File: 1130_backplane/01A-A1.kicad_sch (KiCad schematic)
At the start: 86 parts

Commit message: DN101-DN111 added to backplane schematics, DN111 01B-A1 connections made, 01B-B1 connections to be made when all signals on connectors
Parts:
- removed J1, J10, J11, J12, J13, J14, J15, J16, J17, J18, J19, J2, J20, J21, J22, J23, J24, J25, J26, J27, J28, J29, J3, J30, J31, J32, J33, J34, J35, J36, J37, J38, J39, J4, J40, J41, J42, J43, J44, J45, J46, J47, J48, J49, J5, J50, J51, J52, J53, J54, J55, J56, J57, J58, J59, J6, J60, J61, J62, J63, J64, J65, J66, J67, J68, J69, J7, J70, J71, J72, J73, J74, J75, J76, J77, J78, J79, J8, J80, J81, J82, J83, J84, J85, J86, J9: ~, symbol Connector_Generic:Conn_02x12_Row_Letter_First
- added J? (x86): ~, symbol Connector_Generic:Conn_02x12_Row_Letter_First
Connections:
- net +3V: now also J?.b2 (Pin_b2), J?.b2 (Pin_b2), J?.b2 (Pin_b2), J?.b2 (Pin_b2), J?.b2 (Pin_b2), J?.b2 (Pin_b2), J?.b2 (Pin_b2), J?.b2 (Pin_b2), J?.b2 (Pin_b2), J?.b2 (Pin_b2), J?.b2 (Pin_b2), J?.b2 (Pin_b2), J?.b2 (Pin_b2), J?.b2 (Pin_b2), J?.b2 (Pin_b2), J?.b2 (Pin_b2), J?.b2 (Pin_b2), J?.b2 (Pin_b2), J?.b2 (Pin_b2), J?.b2 (Pin_b2), J?.b2 (Pin_b2), J?.b2 (Pin_b2), J?.b2 (Pin_b2), J?.b2 (Pin_b2), J?.b2 (Pin_b2), J?.b2 (Pin_b2), J?.b2 (Pin_b2), J?.b2 (Pin_b2), J?.b2 (Pin_b2), J?.b2 (Pin_b2), J?.b2 (Pin_b2), J?.b2 (Pin_b2), J?.b2 (Pin_b2), J?.b2 (Pin_b2), J?.b2 (Pin_b2), J?.b2 (Pin_b2), J?.b2 (Pin_b2), J?.b2 (Pin_b2), J?.b2 (Pin_b2), J?.b2 (Pin_b2), J?.b2 (Pin_b2), J?.b2 (Pin_b2), J?.b2 (Pin_b2), J?.b2 (Pin_b2), J?.b2 (Pin_b2), J?.b2 (Pin_b2), J?.b2 (Pin_b2), J?.b2 (Pin_b2), J?.b2 (Pin_b2), J?.b2 (Pin_b2), J?.b2 (Pin_b2), J?.b2 (Pin_b2), J?.b2 (Pin_b2), J?.b2 (Pin_b2), J?.b2 (Pin_b2), J?.b2 (Pin_b2), J?.b2 (Pin_b2), J?.b2 (Pin_b2), J?.b2 (Pin_b2), J?.b2 (Pin_b2), J?.b2 (Pin_b2), J?.b2 (Pin_b2), J?.b2 (Pin_b2), J?.b2 (Pin_b2), J?.b2 (Pin_b2), J?.b2 (Pin_b2), J?.b2 (Pin_b2), J?.b2 (Pin_b2), J?.b2 (Pin_b2), J?.b2 (Pin_b2), J?.b2 (Pin_b2), J?.b2 (Pin_b2), J?.b2 (Pin_b2), J?.b2 (Pin_b2), J?.b2 (Pin_b2), J?.b2 (Pin_b2), J?.b2 (Pin_b2)
- net +6V: now also J?.a10 (Pin_a10), J?.a10 (Pin_a10), J?.a10 (Pin_a10), J?.a10 (Pin_a10), J?.a10 (Pin_a10), J?.a10 (Pin_a10), J?.a10 (Pin_a10), J?.a10 (Pin_a10), J?.a10 (Pin_a10), J?.a10 (Pin_a10), J?.a10 (Pin_a10), J?.a10 (Pin_a10), J?.a10 (Pin_a10), J?.a10 (Pin_a10), J?.a10 (Pin_a10), J?.a10 (Pin_a10), J?.a10 (Pin_a10), J?.a10 (Pin_a10), J?.a10 (Pin_a10), J?.a10 (Pin_a10), J?.a10 (Pin_a10), J?.a10 (Pin_a10), J?.a10 (Pin_a10), J?.a10 (Pin_a10), J?.a10 (Pin_a10), J?.a10 (Pin_a10), J?.a10 (Pin_a10), J?.a10 (Pin_a10), J?.a10 (Pin_a10), J?.a10 (Pin_a10), J?.a10 (Pin_a10), J?.a10 (Pin_a10), J?.a10 (Pin_a10), J?.a10 (Pin_a10), J?.a10 (Pin_a10), J?.a10 (Pin_a10), J?.a10 (Pin_a10), J?.a10 (Pin_a10), J?.a10 (Pin_a10), J?.a10 (Pin_a10), J?.a10 (Pin_a10), J?.a10 (Pin_a10), J?.a10 (Pin_a10), J?.a10 (Pin_a10), J?.a10 (Pin_a10), J?.a10 (Pin_a10), J?.a10 (Pin_a10), J?.a10 (Pin_a10), J?.a10 (Pin_a10), J?.a10 (Pin_a10), J?.a10 (Pin_a10), J?.a10 (Pin_a10), J?.a10 (Pin_a10), J?.a10 (Pin_a10), J?.a10 (Pin_a10), J?.a10 (Pin_a10), J?.a10 (Pin_a10), J?.a10 (Pin_a10), J?.a10 (Pin_a10), J?.a10 (Pin_a10), J?.a10 (Pin_a10), J?.a10 (Pin_a10), J?.a10 (Pin_a10), J?.a10 (Pin_a10), J?.a10 (Pin_a10), J?.a10 (Pin_a10), J?.a10 (Pin_a10), J?.a10 (Pin_a10), J?.a10 (Pin_a10), J?.a10 (Pin_a10), J?.a10 (Pin_a10), J?.a10 (Pin_a10), J?.a10 (Pin_a10), J?.a10 (Pin_a10), J?.a10 (Pin_a10), J?.a10 (Pin_a10), J?.a10 (Pin_a10)
- net -3V: now also J?.a5 (Pin_a5), J?.a5 (Pin_a5), J?.a5 (Pin_a5), J?.a5 (Pin_a5), J?.a5 (Pin_a5), J?.a5 (Pin_a5), J?.a5 (Pin_a5), J?.a5 (Pin_a5), J?.a5 (Pin_a5), J?.a5 (Pin_a5), J?.a5 (Pin_a5), J?.a5 (Pin_a5), J?.a5 (Pin_a5), J?.a5 (Pin_a5), J?.a5 (Pin_a5), J?.a5 (Pin_a5), J?.a5 (Pin_a5), J?.a5 (Pin_a5), J?.a5 (Pin_a5), J?.a5 (Pin_a5), J?.a5 (Pin_a5), J?.a5 (Pin_a5), J?.a5 (Pin_a5), J?.a5 (Pin_a5), J?.a5 (Pin_a5), J?.a5 (Pin_a5), J?.a5 (Pin_a5), J?.a5 (Pin_a5), J?.a5 (Pin_a5), J?.a5 (Pin_a5), J?.a5 (Pin_a5), J?.a5 (Pin_a5), J?.a5 (Pin_a5), J?.a5 (Pin_a5), J?.a5 (Pin_a5), J?.a5 (Pin_a5), J?.a5 (Pin_a5), J?.a5 (Pin_a5), J?.a5 (Pin_a5), J?.a5 (Pin_a5), J?.a5 (Pin_a5), J?.a5 (Pin_a5), J?.a5 (Pin_a5), J?.a5 (Pin_a5), J?.a5 (Pin_a5), J?.a5 (Pin_a5), J?.a5 (Pin_a5), J?.a5 (Pin_a5), J?.a5 (Pin_a5), J?.a5 (Pin_a5), J?.a5 (Pin_a5), J?.a5 (Pin_a5), J?.a5 (Pin_a5), J?.a5 (Pin_a5), J?.a5 (Pin_a5), J?.a5 (Pin_a5), J?.a5 (Pin_a5), J?.a5 (Pin_a5), J?.a5 (Pin_a5), J?.a5 (Pin_a5), J?.a5 (Pin_a5), J?.a5 (Pin_a5), J?.a5 (Pin_a5), J?.a5 (Pin_a5), J?.a5 (Pin_a5), J?.a5 (Pin_a5), J?.a5 (Pin_a5), J?.a5 (Pin_a5), J?.a5 (Pin_a5), J?.a5 (Pin_a5), J?.a5 (Pin_a5), J?.a5 (Pin_a5), J?.a5 (Pin_a5), J?.a5 (Pin_a5), J?.a5 (Pin_a5), J?.a5 (Pin_a5), J?.a5 (Pin_a5)
- net -IO_BIT_0: now also J?.a2 (Pin_a2)
- net -IO_BIT_1: now also J?.b1 (Pin_b1)
- net -IO_BIT_10: now also J?.a7 (Pin_a7)
- net -IO_BIT_11: now also J?.b6 (Pin_b6)
- net -IO_BIT_12: now also J?.a8 (Pin_a8)
- net -IO_BIT_13: now also J?.b8 (Pin_b8)
- net -IO_BIT_14: now also J?.a9 (Pin_a9)
- net -IO_BIT_15: now also J?.b9 (Pin_b9)
- net -IO_BIT_2: now also J?.a3 (Pin_a3)
- net -IO_BIT_3: now also J?.b2 (Pin_b2)
- net -IO_BIT_4: now also J?.a4 (Pin_a4)
- net -IO_BIT_5: now also J?.b3 (Pin_b3)
- net -IO_BIT_6: now also J?.a5 (Pin_a5)
- net -IO_BIT_7: now also J?.b4 (Pin_b4)
- net -IO_BIT_8: now also J?.a6 (Pin_a6)
- net -IO_BIT_9: now also J?.b5 (Pin_b5)
- net GND: now also J?.b7 (Pin_b7), J?.b7 (Pin_b7), J?.b7 (Pin_b7), J?.b7 (Pin_b7), J?.b7 (Pin_b7), J?.b7 (Pin_b7), J?.b7 (Pin_b7), J?.b7 (Pin_b7), J?.b7 (Pin_b7), J?.b7 (Pin_b7), J?.b7 (Pin_b7), J?.b7 (Pin_b7), J?.b7 (Pin_b7), J?.b7 (Pin_b7), J?.b7 (Pin_b7), J?.b7 (Pin_b7), J?.b7 (Pin_b7), J?.b7 (Pin_b7), J?.b7 (Pin_b7), J?.b7 (Pin_b7), J?.b7 (Pin_b7), J?.b7 (Pin_b7), J?.b7 (Pin_b7), J?.b7 (Pin_b7), J?.b7 (Pin_b7), J?.b7 (Pin_b7), J?.b7 (Pin_b7), J?.b7 (Pin_b7), J?.b7 (Pin_b7), J?.b7 (Pin_b7), J?.b7 (Pin_b7), J?.b7 (Pin_b7), J?.b7 (Pin_b7), J?.b7 (Pin_b7), J?.b7 (Pin_b7), J?.b7 (Pin_b7), J?.b7 (Pin_b7), J?.b7 (Pin_b7), J?.b7 (Pin_b7), J?.b7 (Pin_b7), J?.b7 (Pin_b7), J?.b7 (Pin_b7), J?.b7 (Pin_b7), J?.b7 (Pin_b7), J?.b7 (Pin_b7), J?.b7 (Pin_b7), J?.b7 (Pin_b7), J?.b7 (Pin_b7), J?.b7 (Pin_b7), J?.b7 (Pin_b7), J?.b7 (Pin_b7), J?.b7 (Pin_b7), J?.b7 (Pin_b7), J?.b7 (Pin_b7), J?.b7 (Pin_b7), J?.b7 (Pin_b7), J?.b7 (Pin_b7), J?.b7 (Pin_b7), J?.b7 (Pin_b7), J?.b7 (Pin_b7), J?.b7 (Pin_b7), J?.b7 (Pin_b7), J?.b7 (Pin_b7), J?.b7 (Pin_b7), J?.b7 (Pin_b7), J?.b7 (Pin_b7), J?.b7 (Pin_b7), J?.b7 (Pin_b7), J?.b7 (Pin_b7), J?.b7 (Pin_b7), J?.b7 (Pin_b7), J?.b7 (Pin_b7), J?.b7 (Pin_b7), J?.b7 (Pin_b7), J?.b7 (Pin_b7), J?.b7 (Pin_b7), J?.b7 (Pin_b7), J?.b7 (Pin_b7), J?.b7 (Pin_b7), J?.b7 (Pin_b7), J?.b7 (Pin_b7), J?.b7 (Pin_b7), J?.b7 (Pin_b7), J?.b7 (Pin_b7), J?.b7 (Pin_b7), J?.b7 (Pin_b7)

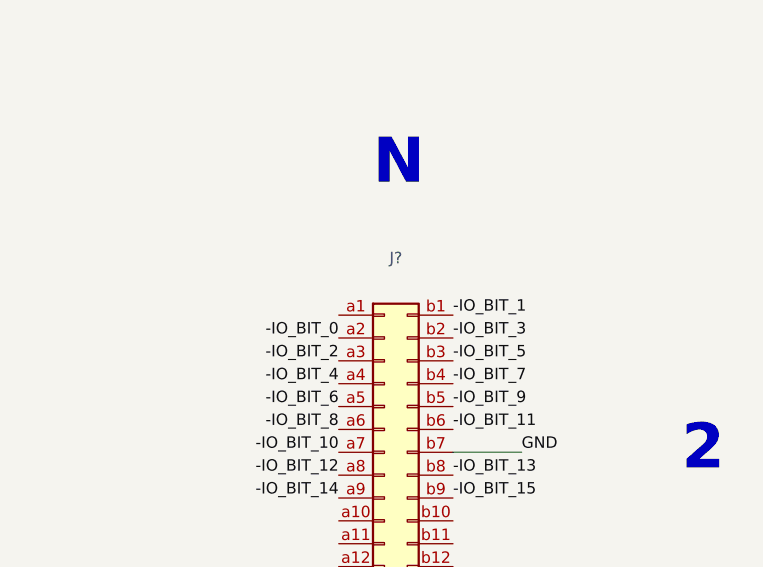
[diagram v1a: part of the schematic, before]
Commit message: Add labels for cable runs, completed tracing for DN111 from previous commit, decided it would be too much work to go back and route later... Completed DN201 page.
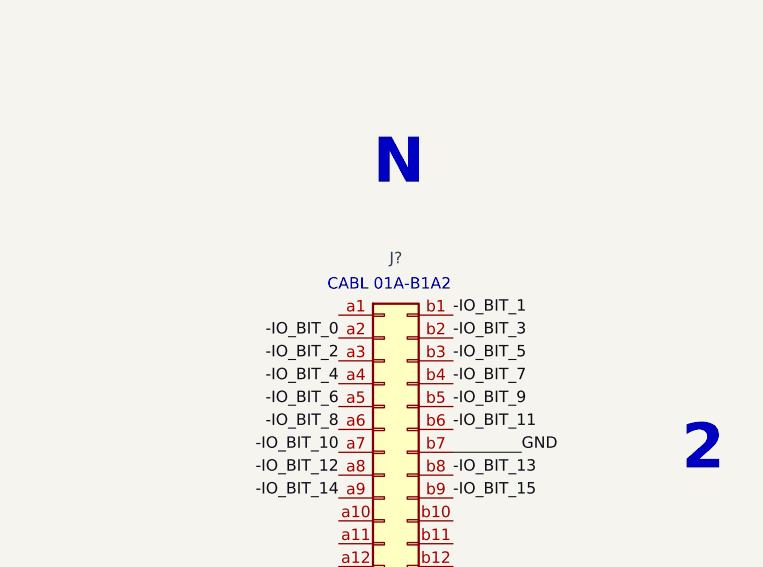
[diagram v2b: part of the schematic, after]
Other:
- note added: "CABL 01A-B1A2"
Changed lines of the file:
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@@
     (effects (font (size 5 5) (thickness 1) bold) (justify left bottom))
+  )
+  (text "CABL 01A-B1A2" (at 793.75 101.6 0)
+    (effects (font (size 1.27 1.27)) (justify left bottom))
   )
   (text "3" (at 833.12 160.02 0)

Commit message: Add labels for bottom T[x] connectors, finished page DU101.
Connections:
- net +3V: no longer J?.b2 (Pin_b2)
- net +6V: no longer J?.a10 (Pin_a10)
- net -3V: no longer J?.a5 (Pin_a5)
- net +U_REG_8_PWR: now reaches J?.a11 (Pin_a11)
- net +U_REG_9_PWR: now reaches J?.a12 (Pin_a12)
- net +XIO_SENSE_ILSW: now reaches J?.a3 (Pin_a3)
- net +XIO_READ: now reaches J?.a7 (Pin_a7)
- net +XIO_CONTROL: now reaches J?.a8 (Pin_a8)
- net +XIO_SENSE_DEVICE: now reaches J?.b9 (Pin_b9)
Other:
- note added: "CABL 01A-B1A5"
- moved on the sheet: J?

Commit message: Fix routing mistake from DU101 for T6, was 01A-A1 to 01A-B1, corrected from 01A-A1 to 01A-C1, finished page DU111.
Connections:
- net +U_REG_13_PWR: now reaches J?.b10 (Pin_b10)
- net +U_REG_14_PWR: now reaches J?.b11 (Pin_b11)
- net +U_REG_15_PWR: now reaches J?.b12 (Pin_b12)
- net +AREA_8: now reaches J?.b3 (Pin_b3)
- net +AREA_6: now reaches J?.a2 (Pin_a2)
- net +XIO_SENSE_RESET_15: now reaches J?.b10 (Pin_b10)
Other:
- note added: "CABL 01A-C1T6"
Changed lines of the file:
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@@
+    (effects (font (size 1.27 1.27)) (justify left bottom))
+  )
+  (text "CABL 01A-C1T6" (at 393.7 393.7 0)
     (effects (font (size 1.27 1.27)) (justify left bottom))
   )
@@
     (effects (font (size 1.27 1.27)) (justify left bottom))
   )
+  (label "+AREA_8" (at 392.43 356.87 90)
+    (effects (font (size 1.27 1.27)) (justify left bottom))
+  )
   (label "GND" (at 370.84 271.78 0)
     (effects (font (size 1.27 1.27)) (justify left bottom))
@@
     (effects (font (size 1.27 1.27)) (justify right bottom))
   )
+  (label "+U_REG_15_PWR" (at 807.72 132.08 0)
+    (effects (font (size 1.27 1.27)) (justify left bottom))
+  )
   (label "GND" (at 434.34 233.68 0)
     (effects (font (size 1.27 1.27)) (justify left bottom))
@@
     (effects (font (size 1.27 1.27)) (justify right bottom))
   )
+  (label "+AREA_6" (at 795.02 220.98 180)
+    (effects (font (size 1.27 1.27)) (justify right bottom))
+  )
   (label "GND" (at 561.34 157.48 0)
     (effects (font (size 1.27 1.27)) (justify left bottom))
@@
     (effects (font (size 1.27 1.27)) (justify right bottom))
   )
+  (label "+U_REG_13_PWR" (at 807.72 127 0)
+    (effects (font (size 1.27 1.27)) (justify left bottom))
+  )
   (label "+3V" (at 307.34 220.98 0)
     (effects (font (size 1.27 1.27)) (justify left bottom))
@@
     (effects (font (size 1.27 1.27)) (justify right bottom))
   )
+  (label "+U_REG_14_PWR" (at 807.72 129.54 0)
+    (effects (font (size 1.27 1.27)) (justify left bottom))
+  )
   (label "+6V" (at 25.4 279.4 180)
     (effects (font (size 1.27 1.27)) (justify right bottom))
@@
     (effects (font (size 1.27 1.27)) (justify right bottom))
   )
+  (label "+XIO_SENSE_RESET_15" (at 807.72 241.3 0)
+    (effects (font (size 1.27 1.27)) (justify left bottom))
+  )
   (label "+6V" (at 279.4 279.4 180)

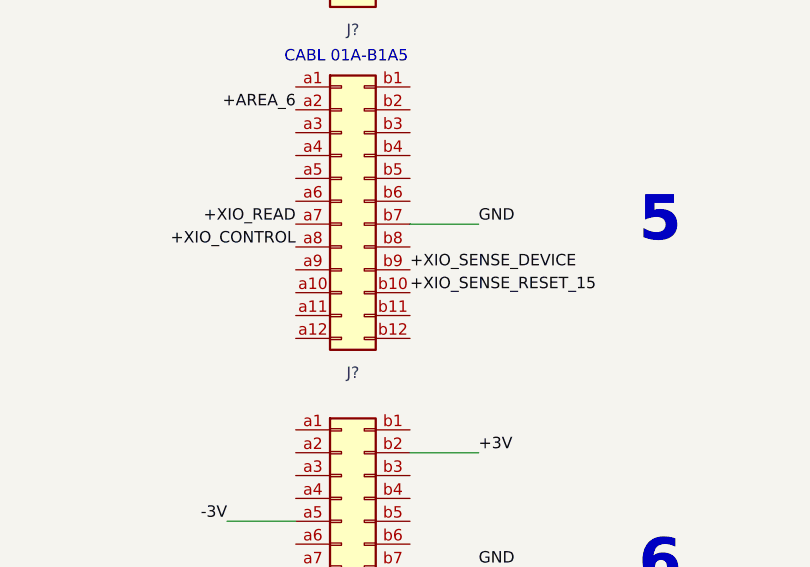
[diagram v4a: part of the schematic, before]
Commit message: Finish page KA101-KA111
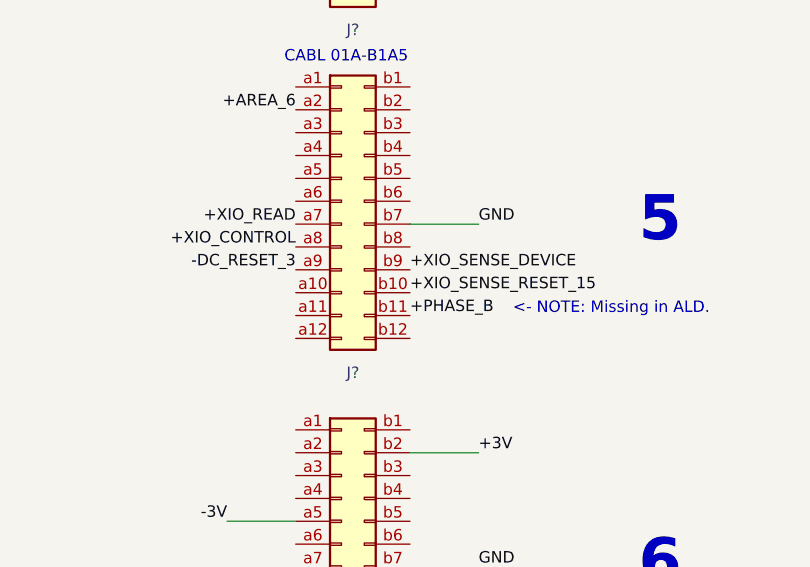
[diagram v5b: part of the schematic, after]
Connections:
- net -DC_RESET_3: now reaches J?.a9 (Pin_a9)
- net +PHASE_B: now reaches J?.b11 (Pin_b11)
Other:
- note added: "<- NOTE: Missing in ALD."
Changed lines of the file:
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@@
     (effects (font (size 5 5) (thickness 1) bold) (justify left bottom))
+  )
+  (text "<- NOTE: Missing in ALD." (at 819.15 243.84 0)
+    (effects (font (size 1.27 1.27)) (justify left bottom))
   )
   (text "K" (at 607.06 90.17 0)
@@
     (effects (font (size 1.27 1.27)) (justify right bottom))
   )
+  (label "-DC_RESET_3" (at 795.02 238.76 180)
+    (effects (font (size 1.27 1.27)) (justify right bottom))
+  )
   (label "-3V" (at 342.9 266.7 180)
     (effects (font (size 1.27 1.27)) (justify right bottom))
@@
     (effects (font (size 1.27 1.27)) (justify left bottom))
   )
+  (label "+PHASE_B" (at 807.72 243.84 0)
+    (effects (font (size 1.27 1.27)) (justify left bottom))
+  )

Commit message: Redo annotations...
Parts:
- gave numbers to parts that had none: 86

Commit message: Finish page KM201-KM211
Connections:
- net +3V: no longer J83.b2 (Pin_b2)
- net +6V: no longer J83.a10 (Pin_a10)
- net -3V: no longer J83.a5 (Pin_a5)
- net -CS_LEVEL_1: now reaches J83.a4 (Pin_a4)
- net -PRINTER_C_S_REQ: now reaches J83.a6 (Pin_a6)
- net +CS_LEVEL_1: now reaches J83.a7 (Pin_a7)
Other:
- note added: "*1"
- note added: "*1: Missing in ALD net listings."
- note added: "CABL 01B-B1B7"
- note removed: "<- NOTE: Missing in ALD."
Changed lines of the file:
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@@
-    (stroke (width 0) (type default) (color 0 0 0 0))
-  )
-  (wire (pts (xy 807.72 182.88) (xy 815.34 182.88))
     (stroke (width 0) (type default) (color 0 0 0 0))
   )
@@
     (stroke (width 0) (type solid) (color 0 0 0 0))
   )
-  (wire (pts (xy 787.4 203.2) (xy 795.02 203.2))
-    (stroke (width 0) (type default) (color 0 0 0 0))
-  )
   (wire (pts (xy 152.4 152.4) (xy 160.02 152.4))
     (stroke (width 0) (type default) (color 0 0 0 0))
@@
     (stroke (width 0) (type solid) (color 0 0 0 0))
   )
-  (wire (pts (xy 787.4 190.5) (xy 795.02 190.5))
-    (stroke (width 0) (type default) (color 0 0 0 0))
-  )
   (wire (pts (xy 478.79 50.8) (xy 478.79 43.18))
     (stroke (width 0) (type default) (color 0 0 0 0))
@@
     (effects (font (size 1.27 1.27)) (justify left bottom))
   )
+  (text "CABL 01B-B1B7" (at 793.75 177.8 0)
+    (effects (font (size 1.27 1.27)) (justify left bottom))
+  )
   (text "A" (at 293.37 365.76 0)
     (effects (font (size 5 5) (thickness 1) bold) (justify left bottom))
@@
     (effects (font (size 5 5) (thickness 1) bold) (justify left bottom))
   )
-  (text "<- NOTE: Missing in ALD." (at 819.15 243.84 0)
+  (text "*1" (at 819.15 243.84 0)
     (effects (font (size 1.27 1.27)) (justify left bottom))
   )
@@
     (effects (font (size 1.27 1.27)) (justify left bottom))
   )
+  (text "*1" (at 773.43 193.04 0)
+    (effects (font (size 1.27 1.27)) (justify left bottom))
+  )
   (text "2" (at 833.12 121.92 0)
     (effects (font (size 5 5) (thickness 1) bold) (justify left bottom))
@@
     (effects (font (size 5 5) (thickness 1) bold) (justify left bottom))
   )
+  (text "*1: Missing in ALD net listings." (at 736.6 355.6 0)
+    (effects (font (size 3 3)) (justify left bottom))
+  )
   (label "+6V" (at 533.4 203.2 180)
     (effects (font (size 1.27 1.27)) (justify right bottom))
@@
     (effects (font (size 1.27 1.27)) (justify left bottom))
   )
-  (label "-3V" (at 787.4 190.5 180)
-    (effects (font (size 1.27 1.27)) (justify right bottom))
-  )
   (label "-IO_BIT_7" (at 807.72 111.76 0)
     (effects (font (size 1.27 1.27)) (justify left bottom))
@@
     (effects (font (size 1.27 1.27)) (justify left bottom))
   )
+  (label "+CS_LEVEL_1" (at 795.02 195.58 180)
+    (effects (font (size 1.27 1.27)) (justify right bottom))
+  )
   (label "-IO_BIT_9" (at 807.72 114.3 0)
     (effects (font (size 1.27 1.27)) (justify left bottom))
@@
     (effects (font (size 1.27 1.27)) (justify left bottom))
   )
-  (label "+3V" (at 815.34 182.88 0)
-    (effects (font (size 1.27 1.27)) (justify left bottom))
-  )
   (label "GND" (at 497.84 309.88 0)
     (effects (font (size 1.27 1.27)) (justify left bottom))
@@
     (effects (font (size 1.27 1.27)) (justify left bottom))
   )
+  (label "-CS_LEVEL_1" (at 795.02 187.96 180)
+    (effects (font (size 1.27 1.27)) (justify right bottom))
+  )
   (label "GND" (at 307.34 271.78 0)
     (effects (font (size 1.27 1.27)) (justify left bottom))
@@
     (effects (font (size 1.27 1.27)) (justify right bottom))
   )
+  (label "-PRINTER_C_S_REQ" (at 795.02 193.04 180)
+    (effects (font (size 1.27 1.27)) (justify right bottom))
+  )
   (label "+XIO_READ" (at 795.02 233.68 180)
     (effects (font (size 1.27 1.27)) (justify right bottom))
@@
     (effects (font (size 1.27 1.27)) (justify left bottom))
   )
-  (label "+6V" (at 787.4 203.2 180)
-    (effects (font (size 1.27 1.27)) (justify right bottom))
-  )
   (label "+6V" (at 342.9 241.3 180)

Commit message: Finish page KM301-KM321
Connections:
- net -INTERRUPT_LEVEL_4: now reaches J40.b6 (Pin_b6)
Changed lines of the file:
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@@
+    (effects (font (size 1.27 1.27)) (justify left bottom))
+  )
+  (label "-INTERRUPT_LEVEL_4" (at 400.05 356.87 90)
     (effects (font (size 1.27 1.27)) (justify left bottom))
   )
